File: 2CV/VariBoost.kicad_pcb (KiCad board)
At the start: 2 copper layers, 75.5 x 46.7 mm, 29 parts, among them P1 CONN_2, P2 CONN_2, P3 CONN_2, P4 CONN_2, P5 CONN_2, Q1 2N2222, Q3 2N2222, Q4 IRGB14C40L, SW1 SWITCH_INV_2RT, U1 CD4011

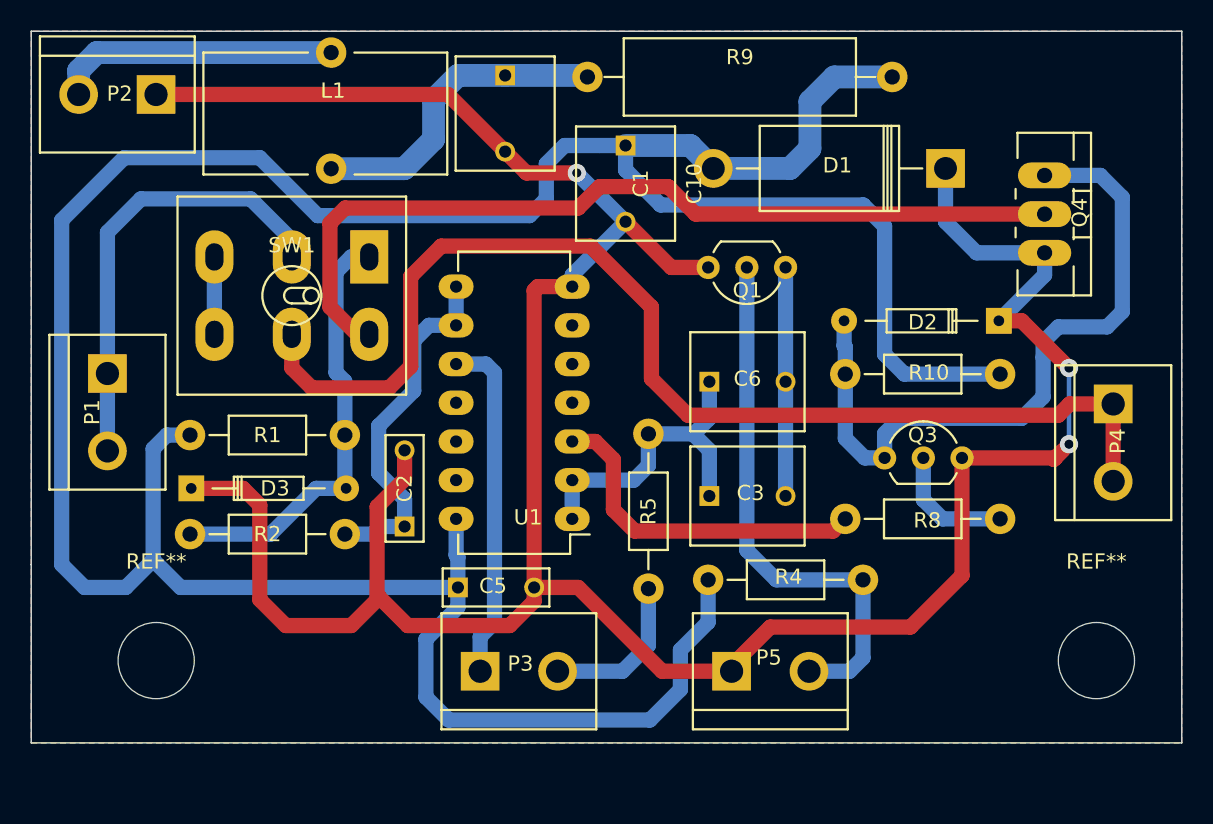
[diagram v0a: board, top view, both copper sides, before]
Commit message: Finish Variboost µC and send to seeed
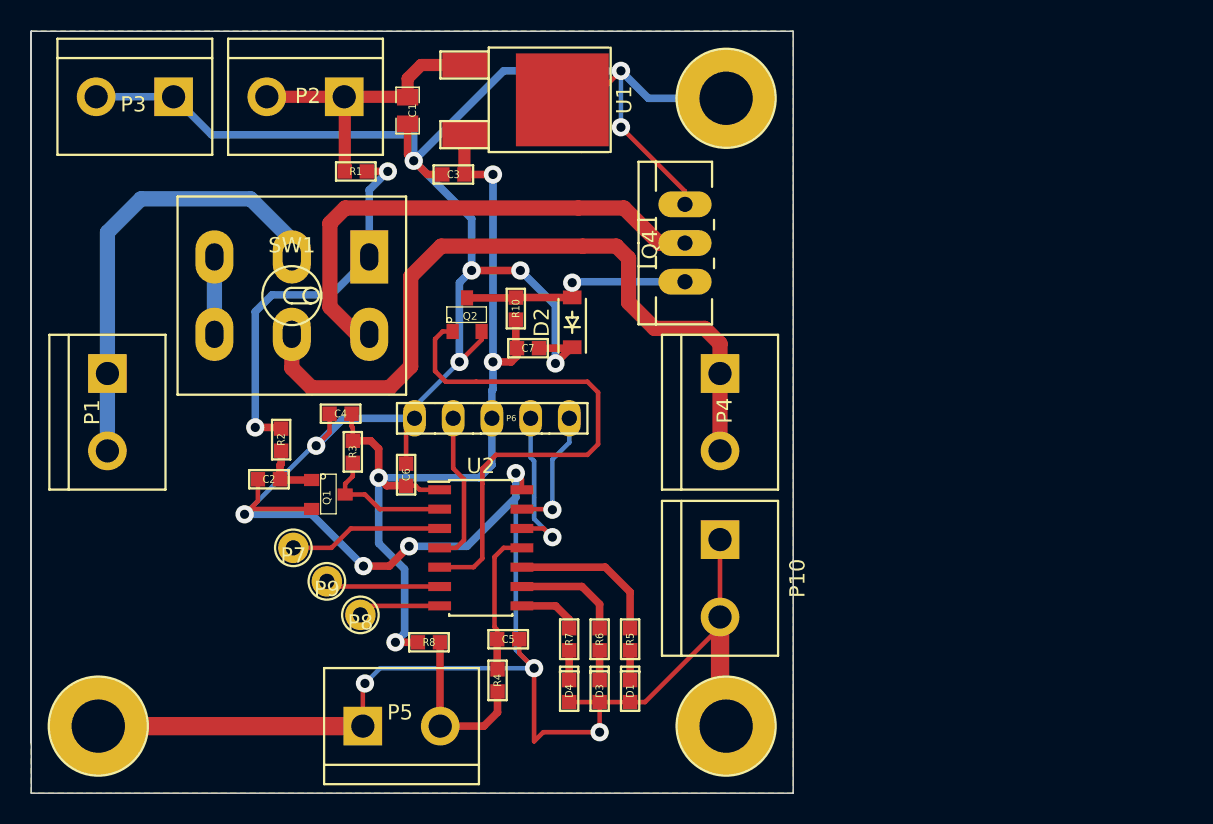
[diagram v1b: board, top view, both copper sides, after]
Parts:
- removed C10: 1u, Capacitors_ThroughHole:C_Rect_L7.5_W6.5_P5
- removed L1: INDUCTOR, Choke_Toroid_ThroughHole:Choke_Toroid_8x16mm_Vertical
- removed Q3: 2N2222, Housings_TO-92:TO-92_Inline_Wide
- removed R9: 100, Resistors_ThroughHole:Resistor_Horizontal_RM20mm
- removed REF** (x2): MountingHole_5mm, Mounting_Holes:MountingHole_5mm
- added C4: 100n, Yame_library:SM0603-MR, F.Cu at (135.3, 85.1)
- added C7: 100n, Yame_library:SM0603-MR, F.Cu at (147.6, 80.8)
- added D4: LED, Yame_library:SM0603-LED-MR, F.Cu at (150.3, 103.3)
- added MountingHole_3.5-6.5+GND: VAL**, Yame_library:MountingHole_3.5-6.5_GND, F.Cu at (119.4, 105.6)
- added MountingHole_3.5-6.5+GND: VAL**, Yame_library:MountingHole_3.5-6.5_GND, F.Cu at (160.6, 105.6)
- added MountingHole_3.5-6.5+GND: VAL**, Yame_library:MountingHole_3.5-6.5_GND, F.Cu at (160.6, 64.4)
- added P10: CONN_2, Connect:bornier2, F.Cu at (160.2, 95.9)
- added P6: CONN_01X05, Yame_library:HE10_14-5C-2.54-MR, F.Cu at (146.5, 85.4)
- added P7: test, Yame_library:Test_Point_T_H, F.Cu at (132.2, 93.9)
- added P8: test, Yame_library:Test_Point_T_H, F.Cu at (136.6, 98.3)
- added P9: test, Yame_library:Test_Point_T_H, F.Cu at (134.4, 96.1)
- added Q2: 2N7002E, Yame_library:SOT23-MR, F.Cu at (143.6, 78.6)
- added R3: 10k, Yame_library:SM0603-MR, F.Cu at (136.1, 87.6)
- added R6: R, Yame_library:SM0603-MR, F.Cu at (152.3, 99.9)
- added R7: R, Yame_library:SM0603-MR, F.Cu at (150.3, 99.9)
- added U2: PIC16F18323_soic, Housings_SOIC:SOIC-14_3.9x8.7mm_Pitch1.27mm, F.Cu at (144.5, 93.9)
- C1: value 1u -> 10u; footprint Capacitors_ThroughHole:C_Rect_L7.5_W6.5_P5 -> Yame_library:SM0805-MR
- C2: value 1n -> 330p; footprint Capacitors_ThroughHole:C_Rect_L7_W2.5_P5 -> Yame_library:SM0603-MR
- C3: footprint Capacitors_ThroughHole:C_Rect_L7.5_W6.5_P5 -> Yame_library:SM0603-MR
- C5: footprint Capacitors_ThroughHole:C_Rect_L7_W2.5_P5 -> Yame_library:SM0603-MR
- C6: value 1u -> 100n; footprint Capacitors_ThroughHole:C_Rect_L7.5_W6.5_P5 -> Yame_library:SM0603-MR
- D1: value 10v_1W -> LED; footprint Diodes_ThroughHole:Diode_DO-201AD_Horizontal_RM15 -> Yame_library:SM0603-LED-MR
- D2: footprint Diodes_ThroughHole:Diode_DO-35_SOD27_Horizontal_RM10 -> Diodes_SMD:SOD-123
- D3: value 10v_1W -> LED; footprint Diodes_ThroughHole:Diode_DO-35_SOD27_Horizontal_RM10 -> Yame_library:SM0603-LED-MR
- Q1: value 2N2222 -> 2N7002E; footprint Housings_TO-92:TO-92_Inline_Wide -> Yame_library:SOT23-MR
- R1, R10, R2, R5, R8: footprint Resistors_ThroughHole:Resistor_Horizontal_RM10mm -> Yame_library:SM0603-MR
- R4: value 10k -> 100; footprint Resistors_ThroughHole:Resistor_Horizontal_RM10mm -> Yame_library:SM0603-MR
- U1: value CD4011 -> 7805_SOT252; footprint Housings_DIP:DIP-14_W7.62mm_LongPads -> TO_SOT_Packages_SMD:TO-252-2Lead
- moved P3 45.3 mm to (121.8, 64.3), turned to 180 degrees
- moved D1 40.1 mm to (154.3, 103.3), turned to 90 degrees
- moved Q1 33.5 mm to (134.5, 90.4), turned to 270 degrees
- moved R8 33.4 mm to (141.1, 100.1), turned to 180 degrees
- moved D3 29.9 mm to (152.3, 103.3), turned to 90 degrees
- moved U1 28.4 mm to (143.5, 64.5), turned to 270 degrees
- moved D2 28.0 mm to (150.5, 79.1), turned to 90 degrees
- moved R10 27.0 mm to (146.8, 78.2), turned to 270 degrees
- moved C3 27.0 mm to (142.7, 69.4), turned to 180 degrees
- moved P4 25.9 mm to (160.2, 85.0)
- moved P5 24.5 mm to (139.3, 105.6)
- moved Q4 23.7 mm to (157.9, 73.9), turned to 90 degrees
- moved C6 20.8 mm to (139.6, 89.1), turned to 90 degrees
- moved R4 20.0 mm to (145.6, 102.6), turned to 270 degrees
- moved R1 18.2 mm to (136.3, 69.2)
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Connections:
- C1 pad 1: VCC -> /+12V
- C3 pad 1: Net-(C3-Pad1) -> /+5V
- C3 pad 2: Net-(C3-Pad2) -> GND
- C5 pad 1: /Vref -> Net-(C5-Pad1)
- C6 pad 1: Net-(C3-Pad1) -> /+5V
- C6 pad 2: Net-(C3-Pad2) -> GND
- D1 pad 2: /Vref -> Net-(D1-Pad2)
- P2 pad 1: GND -> /+12V
- P2 pad 2: Net-(L1-Pad1) -> /+12V
- P3 pad 1: Net-(P3-Pad1) -> GND
- P3 pad 2: Net-(P3-Pad2) -> GND
- Q1 pad 1: Net-(C3-Pad2) -> Net-(C2-Pad1)
- Q1 pad 2: Net-(P5-Pad2) -> GND
- Q1 pad 3: GND -> Net-(Q1-Pad3)
- R1 pad 1: /Vref -> /+12V
- R1 pad 2: Net-(D3-Pad2) -> Net-(R1-Pad2)
- R10 pad 2: /Vref -> /+5V
- R2 pad 1: Net-(D3-Pad2) -> Net-(R1-Pad2)
- R4 pad 1: /Vref -> Net-(C5-Pad1)
- R5 pad 1: Net-(P3-Pad2) -> Net-(D1-Pad2)
- R5 pad 2: Net-(C3-Pad1) -> Net-(R5-Pad2)
- R8 pad 1: Net-(R8-Pad1) -> Net-(P5-Pad2)
- R8 pad 2: Net-(Q3-Pad2) -> /+5V
- SW1 pad 1: Net-(D3-Pad2) -> Net-(R1-Pad2)
- U1 pad 1: Net-(C3-Pad1) -> /+12V
- U1 pad 2: Net-(C3-Pad1) -> GND
- U1 pad 3: Net-(R8-Pad1) -> /+5V
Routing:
- net /Vref: track 202.1 -> 0.00 mm
- net /+5V: track 0.00 -> 58.7 mm, vias 0 -> 4
- net GND: track 189.3 -> 238.8 mm, vias 3 -> 15
- net Net-(Q2-Pad1): track 0.00 -> 35.3 mm
- net Net-(D2-Pad2): track 46.7 -> 15.3 mm, vias 0 -> 1
- net Net-(P4-Pad1): track 76.7 -> 49.5 mm
- net Net-(D3-Pad2): track 28.5 -> 1.95 mm
- net Net-(R1-Pad2): track 0.00 -> 25.8 mm, vias 0 -> 3
- net Net-(P5-Pad2): track 36.0 -> 11.0 mm
- net Net-(Q4-Pad2): track 57.5 -> 33.5 mm
- net Net-(P3-Pad1): track 22.7 -> 0.00 mm
- net Net-(R8-Pad1): track 22.6 -> 0.00 mm
- net Net-(C3-Pad1): track 21.4 -> 0.00 mm
- net VCC: track 20.9 -> 0.00 mm
- net Net-(C2-Pad1): track 23.7 -> 4.00 mm
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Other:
- board size 75.5 x 46.7 mm -> 50 x 50 mm
- board text removed: "delay OFF"
